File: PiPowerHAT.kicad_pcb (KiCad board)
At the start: 2 copper layers, 65 x 56 mm, 34 parts, among them J1 2444, J3 Conn_01x02, J6 Raspberry_Pi_2_3, J8 2444, Q1 AO3401A, Q2 MMDT5401, Q3 AO3401A, U1 XL4015

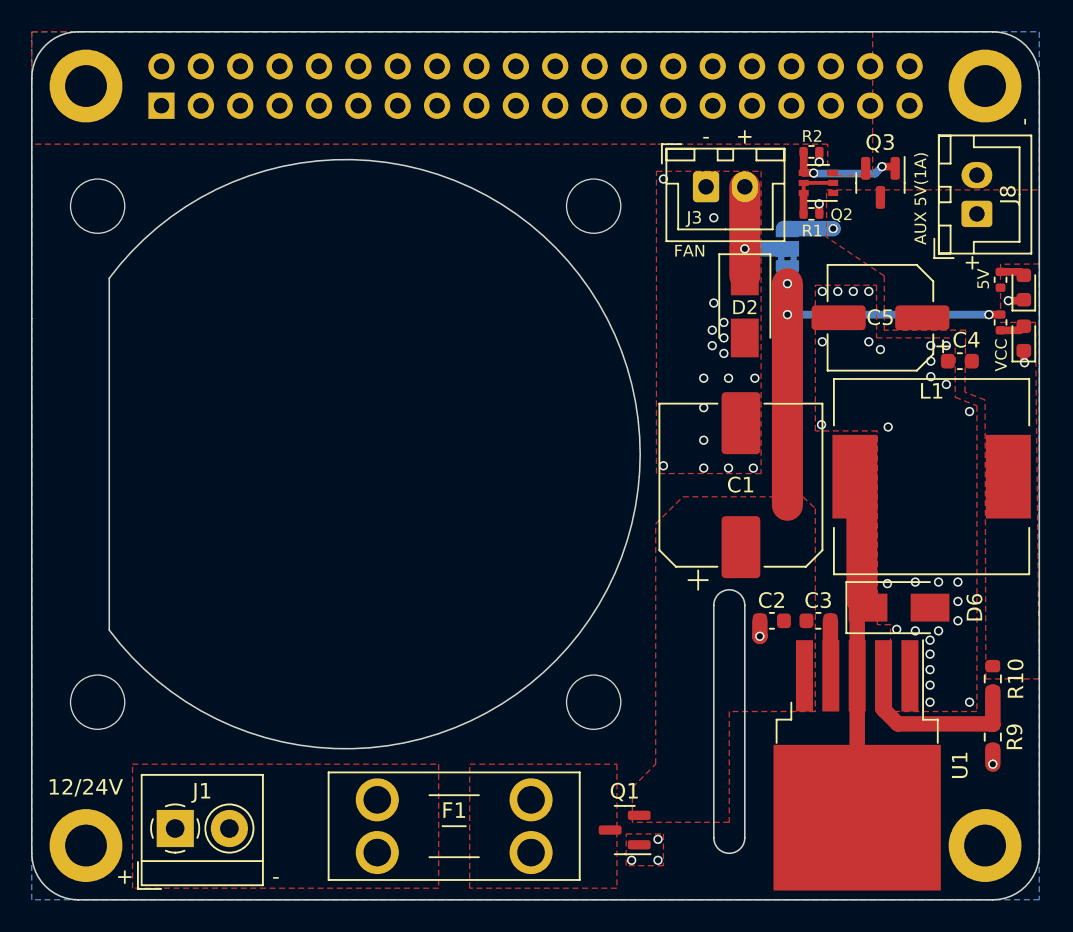
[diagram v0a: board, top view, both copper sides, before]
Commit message: PCBway export and minor changes
V0.1.1 files generated for PCBway with B.Mask included.
Dot added to Pin 1 on F.silk
Added Metadata to work with PCBway BOM
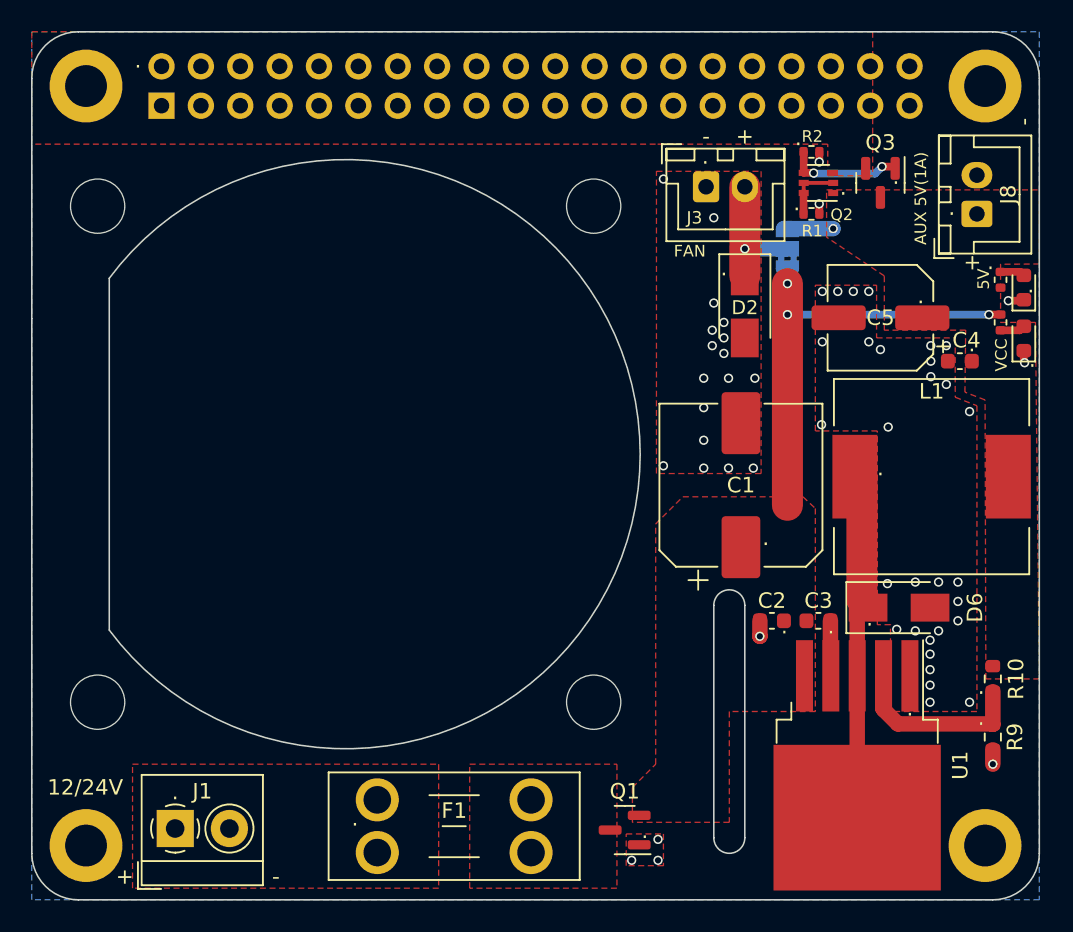
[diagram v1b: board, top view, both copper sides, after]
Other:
- board text added: "."
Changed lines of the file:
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@@
     (pad_to_mask_clearance 0)
     (pcbplotparams
-      (layerselection 0x00010bc_ffffffff)
+      (layerselection 0x00010fc_ffffffff)
       (disableapertmacros false)
       (usegerberextensions false)
@@
     (effects (font (size 1 1) (thickness 0.15)))
   )
+  (gr_text "." (at 136.8 91.6) (layer "F.SilkS")
+    (effects (font (size 1 1) (thickness 0.15)))
+  )
+  (gr_text "." (at 134.7 60.1) (layer "F.SilkS")
+    (effects (font (size 1 1) (thickness 0.15)))
+  )
+  (gr_text "." (at 141 62.6) (layer "F.SilkS")
+    (effects (font (size 1 1) (thickness 0.15)))
+  )
+  (gr_text "." (at 146.5 97.5) (layer "F.SilkS")
+    (effects (font (size 1 1) (thickness 0.15)))
+  )
   (gr_text "+" (at 131.25 60) (layer "F.SilkS")
+    (effects (font (size 1 1) (thickness 0.15)))
+  )
+  (gr_text "." (at 133.8 91.6) (layer "F.SilkS")
+    (effects (font (size 1 1) (thickness 0.15)))
+  )
+  (gr_text "." (at 149.8 74.4) (layer "F.SilkS")
+    (effects (font (size 1 1) (thickness 0.15)))
+  )
+  (gr_text "." (at 124.8 104.8) (layer "F.SilkS")
+    (effects (font (size 1 1) (thickness 0.15)))
+  )
+  (gr_text "." (at 139.3 91.1) (layer "F.SilkS")
+    (effects (font (size 1 1) (thickness 0.15)))
+  )
+  (gr_text "." (at 147.1 68.1) (layer "F.SilkS")
     (effects (font (size 1 1) (thickness 0.15)))
   )
@@
     (effects (font (size 0.75 0.75) (thickness 0.15)))
   )
+  (gr_text "." (at 94.5 102.3) (layer "F.SilkS")
+    (effects (font (size 1 1) (thickness 0.15)))
+  )
+  (gr_text "." (at 140 81.4) (layer "F.SilkS")
+    (effects (font (size 1 1) (thickness 0.15)))
+  )
   (gr_text "-" (at 128.75 60) (layer "F.SilkS")
+    (effects (font (size 1 1) (thickness 0.15)))
+  )
+  (gr_text "." (at 92.1 55.1) (layer "F.SilkS")
     (effects (font (size 1 1) (thickness 0.15)))
   )
@@
     (effects (font (size 1 1) (thickness 0.15)))
   )
+  (gr_text "." (at 146.5 95.5) (layer "F.SilkS")
+    (effects (font (size 1 1) (thickness 0.15)))
+  )
   (gr_text "FAN" (at 127.7 67.4) (layer "F.SilkS")
     (effects (font (size 0.75 0.75) (thickness 0.15)))
   )
+  (gr_text "." (at 129.9 68.5) (layer "F.SilkS")
+    (effects (font (size 1 1) (thickness 0.15)))
+  )
   (gr_text "+" (at 91.25 107.75) (layer "F.SilkS")
     (effects (font (size 1 1) (thickness 0.15)))
   )
+  (gr_text "." (at 142.6 70.3) (layer "F.SilkS")
+    (effects (font (size 1 1) (thickness 0.15)))
+  )
+  (gr_text "." (at 145.9 73.4) (layer "F.SilkS")
+    (effects (font (size 1 1) (thickness 0.15)))
+  )
+  (gr_text "." (at 132.6 85.9) (layer "F.SilkS")
+    (effects (font (size 1 1) (thickness 0.15)))
+  )
+  (gr_text "." (at 141.9 96.9) (layer "F.SilkS")
+    (effects (font (size 1 1) (thickness 0.15)))
+  )
+  (gr_text "." (at 144.6 64.6) (layer "F.SilkS")
+    (effects (font (size 1 1) (thickness 0.15)))
+  )
   (gr_text "-" (at 101 107.75) (layer "F.SilkS")
     (effects (font (size 1 1) (thickness 0.15)))
@@
     (effects (font (size 1 1) (thickness 0.15)))
   )
+  (gr_text "." (at 134.6 64.3) (layer "F.SilkS")
+    (effects (font (size 1 1) (thickness 0.15)))
+  )
+  (gr_text "." (at 149.7 69.6) (layer "F.SilkS")
+    (effects (font (size 1 1) (thickness 0.15)))
+  )
+  (gr_text "." (at 128.7 61.3) (layer "F.SilkS")
+    (effects (font (size 1 1) (thickness 0.15)))
+  )
+  (gr_text "." (at 106.1 104) (layer "F.SilkS")
+    (effects (font (size 1 1) (thickness 0.15)))
+  )
+  (gr_text "." (at 137.6 63.3) (layer "F.SilkS")
+    (effects (font (size 1 1) (thickness 0.15)))
+  )

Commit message: bug fixes
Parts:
- D3, D5: value C72038 -> 2.3V 20mA
- Q1, Q3: value AO3401A -> 30V 4A 44mΩ
- Q2: value MMDT5401 -> 50nA 150V 200mW 200mA
- moved R2 6.43 mm to (141.9, 60.4), turned to 180 degrees
- moved Q2 2.00 mm to (138.0, 63.0)
- moved R1 1.51 mm to (135.8, 63.5), turned to -90 degrees
- moved Q3 1.50 mm to (141.5, 63.0)
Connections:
- C2 pad 1: unconnected-(C2-Pad1) -> VCC
- Q2 pad 3: 5V_PI -> Net-(Q2-Pad3)
- Q2 pad 4: Net-(Q2-Pad4) -> 5V_PI
- Q3 pad 1: Net-(Q2-Pad4) -> Net-(Q2-Pad3)
- R2 pad 1: Net-(Q2-Pad4) -> Net-(Q2-Pad3)
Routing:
- net Net-(Q2-Pad4): track 7.46 -> 0.00 mm, vias 2 -> 0
- net Net-(Q2-Pad3): track 0.00 -> 5.83 mm, vias 0 -> 2
